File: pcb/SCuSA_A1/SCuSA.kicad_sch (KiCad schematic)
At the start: 9 parts, among them U1 LM27762, U102 AD8418

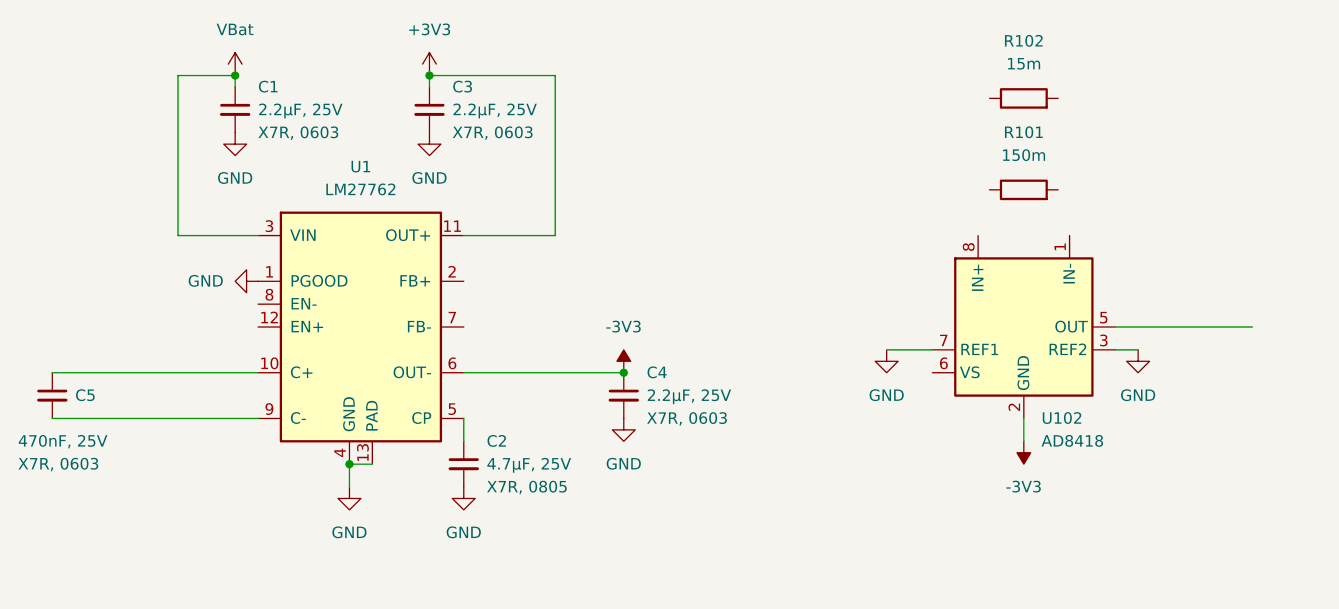
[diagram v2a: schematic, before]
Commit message: Add power supply
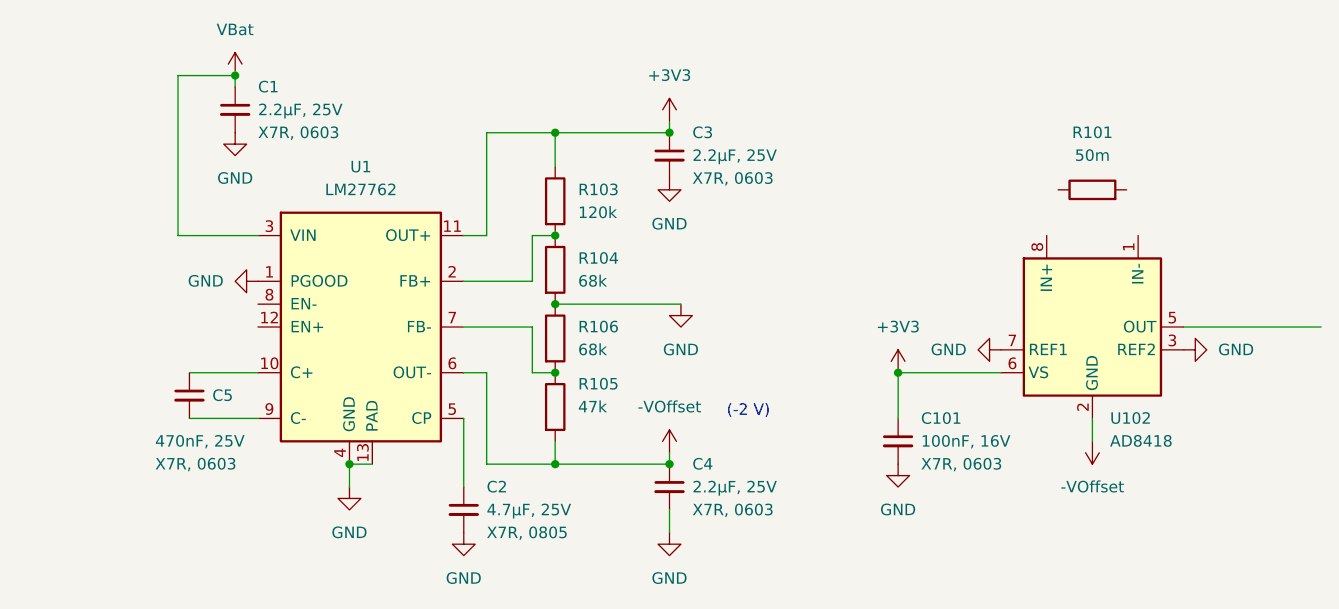
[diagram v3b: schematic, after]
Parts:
- removed R102: 15m, symbol Device:R
- added C101: 100nF,16V,X7R,0603, Capacitor_SMD:C_0603_1608Metric_Pad1.08x0.95mm_HandSolder, symbol Capacitor_User:100nF,16V,X7R,0603
- added R103: 120k,0603, Resistor_SMD:R_0603_1608Metric_Pad0.98x0.95mm_HandSolder, symbol Resistor_User:120k,0603
- added R104, R106: 68k,0603, Resistor_SMD:R_0603_1608Metric_Pad0.98x0.95mm_HandSolder, symbol Resistor_User:68k,0603
- added R105: 120k,0603, Resistor_SMD:R_0603_1608Metric_Pad0.98x0.95mm_HandSolder, symbol Resistor_User:47k,0603
- R101: value 150m -> 50m
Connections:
- net +3V3: now also U102.6 (VS), C101.1, R103.1
- net GND: now also C101.2, R104.2, R106.1
- net at U1.2 (FB+): now also R103.2, R104.1
- net at U1.7 (FB-): now also R105.1, R106.2
- net -3V3: no longer names the net of C4.1, U1.6 (OUT-)
- net -3V3: now also R105.2; no longer U102.2 (GND)
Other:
- note added: "(-2 V)"
- moved on the sheet: C2, C3, C4, C5, R101, U102

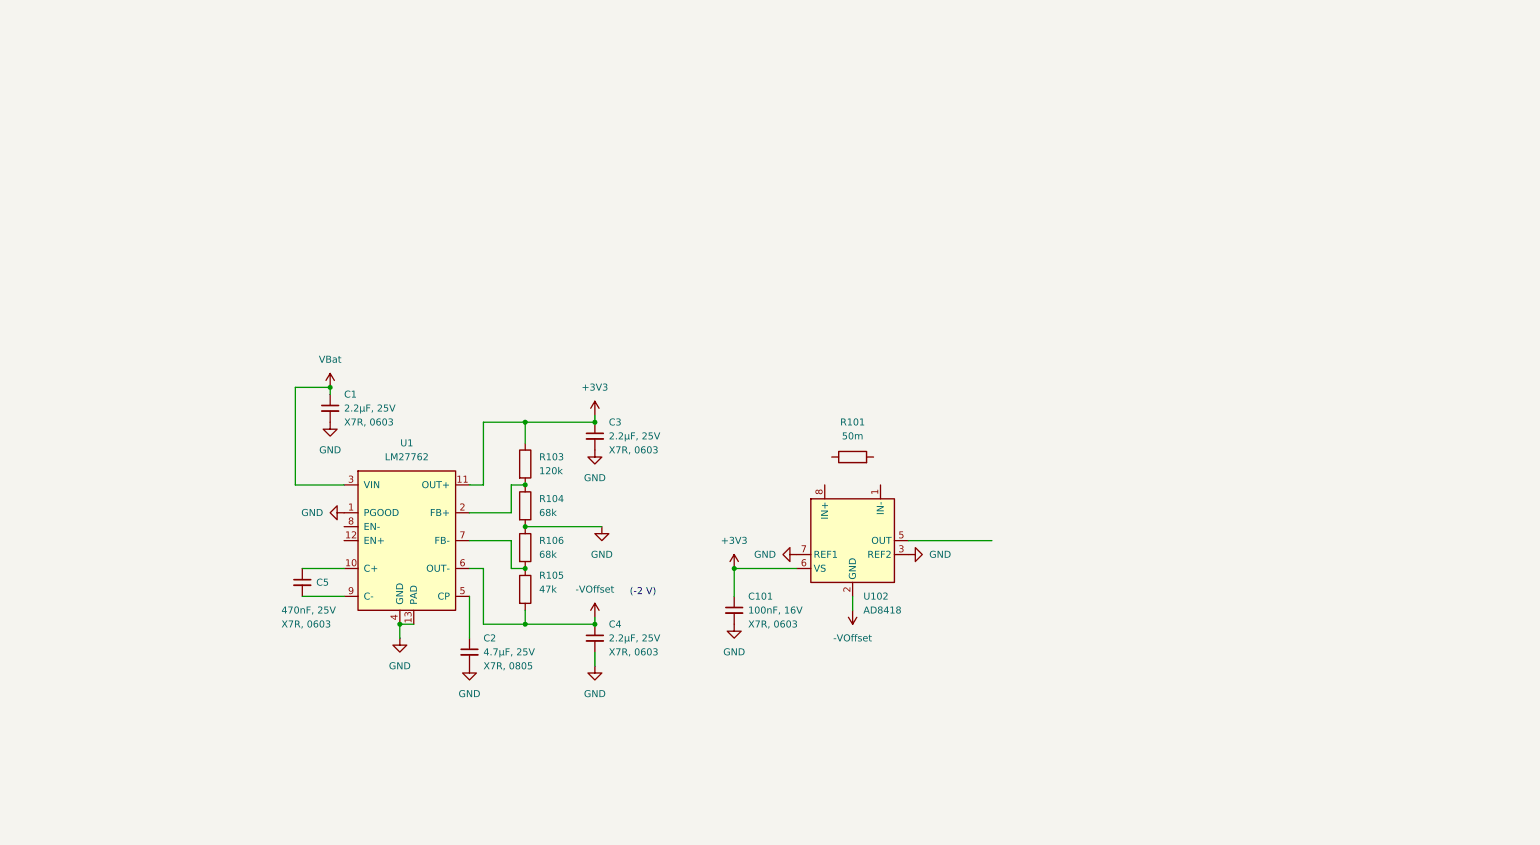
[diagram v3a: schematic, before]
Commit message: Add battery circuit
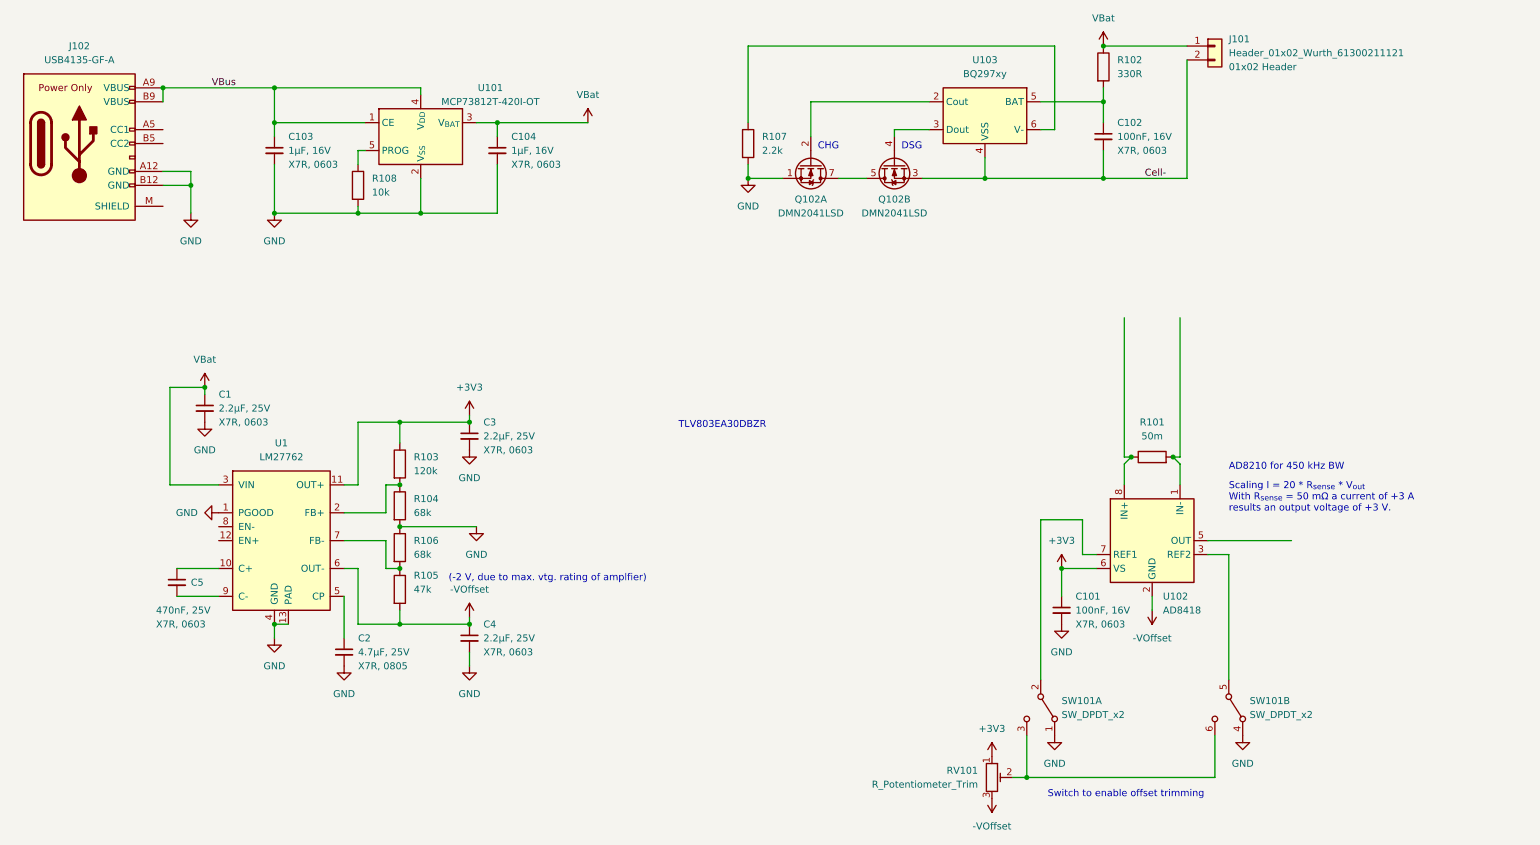
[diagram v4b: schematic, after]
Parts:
- added C102: 100nF,16V,X7R,0603, Capacitor_SMD:C_0603_1608Metric_Pad1.08x0.95mm_HandSolder, symbol Capacitor_User:100nF,16V,X7R,0603
- added C103, C104: 1uF,16V,X7R,0603, Capacitor_SMD:C_0603_1608Metric_Pad1.08x0.95mm_HandSolder, symbol Capacitor_User:1uF,16V,X7R,0603
- added J101: Header_01x02_Wurth_61300211121, Connector_PinHeader_2.54mm:PinHeader_1x02_P2.54mm_Vertical, symbol Connector_User:Header_01x02_Wurth_61300211121
- added J102: USB4135-GF-A, Connector_User:USB-C_Receptacle_GTC_USB4135-GF-A, symbol Connector_User:USB4135-GF-A
- added Q102: DMN2041LSD, Package_SO:SOIC-8_3.9x4.9mm_P1.27mm, symbol Transistor_FET_User:DMN2041LSD
- added R102: 330R,0603, Resistor_SMD:R_0603_1608Metric_Pad0.98x0.95mm_HandSolder, symbol Resistor_User:330R,0603
- added R107: 2.2k,0603, Resistor_SMD:R_0603_1608Metric_Pad0.98x0.95mm_HandSolder, symbol Resistor_User:2.2k,0603
- added R108: 10k,0603, Resistor_SMD:R_0603_1608Metric_Pad0.98x0.95mm_HandSolder, symbol Resistor_User:10k,0603
- added RV101: R_Potentiometer_Trim, symbol Device:R_Potentiometer_Trim
- added SW101: SW_DPDT_x2, symbol Switch:SW_DPDT_x2
- added U101: MCP73812T-420I-OT, Package_TO_SOT_SMD:SOT-23-5, symbol Battery_Management:MCP73812T-420I-OT
- added U103: BQ297xy, Package_SON:WSON-6_1.5x1.5mm_P0.5mm, symbol Battery_Management:BQ297xy
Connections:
- net +3V3: now also RV101.1
- net GND: now also C103.2, C104.2, J102.A12 (GND), J102.B12 (GND), Q102.1 (S1), R107.2, R108.2, SW101.1 (A), SW101.4 (A), U101.2 (V_{SS}); no longer U102.3 (REF2), U102.7 (REF1)
- net VBat: now also C104.1, J101.1 (Pin_1), R102.1, U101.3 (V_{BAT})
- net at U102.1 (IN-): now also R101.2
- net at U102.8 (IN+): now also R101.1
- new net: SW101.5 (B), U102.3 (REF2)
- new net: SW101.2 (B), U102.7 (REF1)
- new net: R108.1, U101.5 (PROG)
- new net: R107.1, U103.6 (V-)
- new net: RV101.2, SW101.3 (C), SW101.6 (C)
- new net: Q102.2 (G1), U103.2 (Cout)
- new net: Q102.4 (G2), U103.3 (Dout)
- new net: C102.1, R102.2, U103.5 (BAT)
- new net: Q102.5 (D2), Q102.6 (D2), Q102.7 (D1), Q102.8 (D1)
- new net Cell-: C102.2, J101.2 (Pin_2), Q102.3 (S2), U103.4 (VSS)
- new net VBus: C103.1, J102.A9 (VBUS), J102.B9 (VBUS), U101.1 (CE), U101.4 (V_{DD})
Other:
- note added: "(-2 V, due to max. vtg. rating of amplfier)"
- note added: "AD8210 for 450 kHz BW"
- note added: "CHG"
- note added: "DSG"
- note added: "Scaling I = 20 * R_{sense} * V_{out} With R_{sense} = 50 mΩ a current of +3 A results an output voltage of +3 V."
- note added: "Switch to enable offset trimming"
- note added: "TLV803EA30DBZR"
- note removed: "(-2 V)"
- moved on the sheet: C1, C101, C2, C3, C4, C5, R101, R103, R104, R105, R106, U1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

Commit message: Work on battery charger
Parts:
- removed J101: Header_01x02_Wurth_61300211121, Connector_PinHeader_2.54mm:PinHeader_1x02_P2.54mm_Vertical, symbol Connector_User:Header_01x02_Wurth_61300211121
- added D101: 150080SS75000, LED_SMD:LED_0805_2012Metric_Pad1.15x1.40mm_HandSolder, symbol LED_User:150080SS75000
- added F101: 0ZCJ0110FF2E, Fuse:Fuse_1206_3216Metric_Pad1.42x1.75mm_HandSolder, symbol Fuse_User:0ZCJ0110FF2E
- added J105: JST_S2B-PH-K-x, Connector_JST:JST_PH_S2B-PH-K_1x02_P2.00mm_Horizontal, symbol Connector_User:JST_S2B-PH-K-x
- added JP101, JP102: SolderJumper_2_Bridged, symbol Jumper:SolderJumper_2_Bridged
- added R109, R110: 5.1M,0603, Resistor_SMD:R_0603_1608Metric_Pad0.98x0.95mm_HandSolder, symbol Resistor_User:5.1M,0603
- added R111, R112: 5.1k,0603, Resistor_SMD:R_0603_1608Metric_Pad0.98x0.95mm_HandSolder, symbol Resistor_User:5.1k,0603
- added R113: 10k,0603, Resistor_SMD:R_0603_1608Metric_Pad0.98x0.95mm_HandSolder, symbol Resistor_User:10k,0603
- added SW102: SW_SPST, symbol Switch:SW_SPST
- added U104: TLV803EA30DBZR, Package_TO_SOT_SMD:SOT-23, symbol Power_Supervisor_User:TLV803EA30DBZR
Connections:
- net Cell-: now also J105.2 (Pin_2), R109.2
- net GND: now also R110.2, R111.2, R112.2, U104.1 (GND)
- net VBat: now also J105.1 (Pin_1), SW102.1 (A); no longer C1.1, U1.3 (VIN)
- net VBus: now also F101.2; no longer J102.A9 (VBUS), J102.B9 (VBUS)
- net at Q102.2 (G1), U103.2 (Cout): now also R110.1
- net at Q102.4 (G2), U103.3 (Dout): now also R109.1
- net at U1.12 (EN+): now also JP102.2 (B)
- net at U1.8 (EN-): now also JP101.2 (B)
- net at J102.A5 (CC1): now also R111.1
- net at J102.B5 (CC2): now also R112.1
- new net: D101.2 (A), R113.2
- new net: D101.1 (K), U104.2 (~{RESET})
- new net: F101.1, J102.A9 (VBUS), J102.B9 (VBUS)
- new net VBat_SW: C1.1, JP101.1 (A), JP102.1 (A), R113.1, SW102.2 (B), U1.3 (VIN), U104.3 (VDD)
- no-connect marks 0 -> 1
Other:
- note added: "+3,3 V Linear Regulator Charge Pump Inverter & -2 V Linear Regulator"
- note added: "Battery Charger"
- note added: "Battery Protection"
- note added: "Cell+"
- note added: "Charge"
- note added: "Current Sense Amplifier"
- note added: "Discharge"
- note added: "Low Battery Warning"
- note added: "Pack-"
- note added: "Switch to enable / disable offset trimming"
- note removed: "CHG"
- note removed: "DSG"
- note removed: "Switch to enable offset trimming"
- note removed: "TLV803EA30DBZR"
- moved on the sheet: C1, C102, C103, C104, C2, C3, C4, C5, Q102A, Q102B, R102, R103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
